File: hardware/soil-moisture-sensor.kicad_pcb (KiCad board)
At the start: 4 copper layers, 185.3 x 23 mm, 34 parts, among them J1 USB_B_Micro, Q1 Q_NPN_BEC, Q2 Q_NPN_BEC, SW1 SW_Push, SW2 SW_Push, U2 CP2102N-Axx-xQFN24, U3 ESP32-WROOM-32D

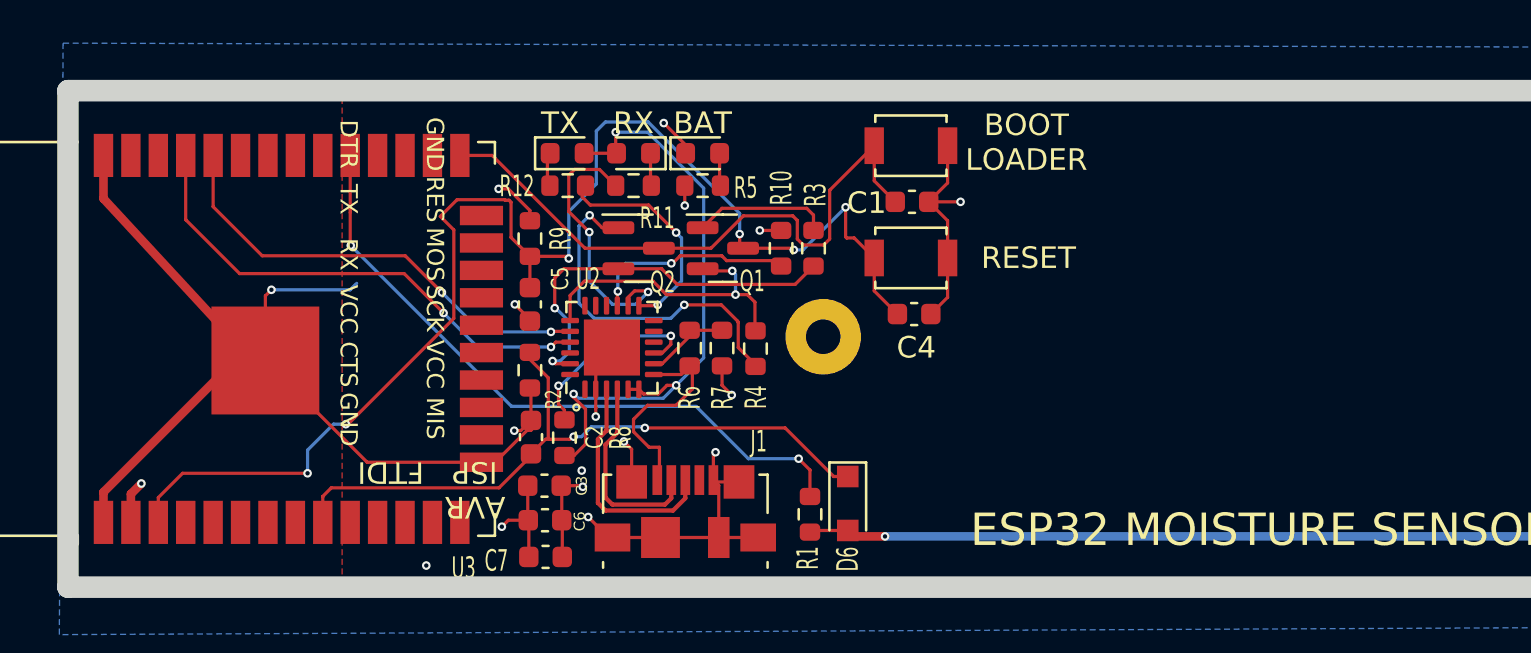
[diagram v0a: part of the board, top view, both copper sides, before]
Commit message: added debug header and fixed more drc issues
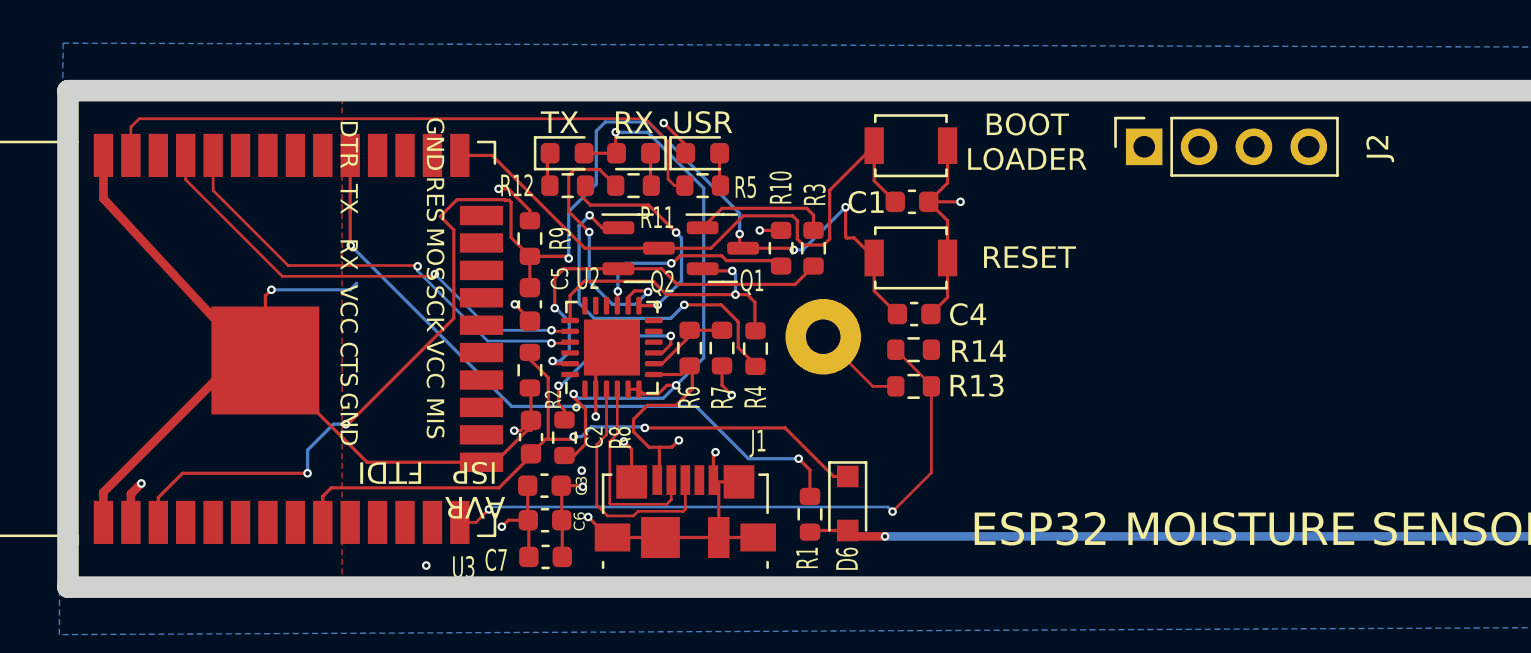
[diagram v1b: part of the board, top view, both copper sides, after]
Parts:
- added J2: Conn_01x04_Male, Connector_PinSocket_2.54mm:PinSocket_1x04_P2.54mm_Vertical, F.Cu at (115.2, 105.3)
- added R13: 10k, Resistor_SMD:R_0603_1608Metric, F.Cu at (104.5, 116.4)
- added R14: 10k, Resistor_SMD:R_0603_1608Metric, F.Cu at (104.5, 114.7)
- R11, R12, R5: value 2k -> 220R
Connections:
- R5 pad 1: +BATT -> /IO23
- U2 pad 20: /RXD -> /ESP_TXD0
- U2 pad 21: /TXD -> /ESP_RXD0
- U3 pad 14: unconnected-(U3-Pad14) -> Net-(U3-Pad14)
- U3 pad 34: /RXD -> /ESP_RXD0
- U3 pad 35: /TXD -> /ESP_TXD0
- U3 pad 37: unconnected-(U3-Pad37) -> /IO23
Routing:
- net /ESP_TXD0: track 0.00 -> 60.5 mm, vias 0 -> 2
- net /ESP_RXD0: track 0.00 -> 57.0 mm, vias 0 -> 2
- net +5V: track 9.92 -> 40.6 mm, vias 0 -> 1
- net /IO23: track 0.00 -> 29.4 mm
- net Net-(U3-Pad14): track 0.00 -> 29.4 mm, vias 0 -> 2
- net /TXD: track 23.3 -> 0.00 mm, vias 2 -> 0
- net /RXD: track 21.3 -> 0.00 mm, vias 2 -> 0
- net +BATT: track 24.9 -> 28.3 mm, vias 4 -> 3
- net /USB_P: track 10.7 -> 11.4 mm
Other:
- board text added: "USR"
- board text removed: "BAT"
